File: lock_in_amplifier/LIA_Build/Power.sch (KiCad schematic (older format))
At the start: 52 parts, among them J1 vref-in, J2 vref, J3 V-IN, J4 GND, J5 V+IN, J6 +5V, J7 +3V3, J8 -5V, Q1 2N7000, Q2 2N7000, U1 OP1177, U2 ?, U3 ?, U4 ?

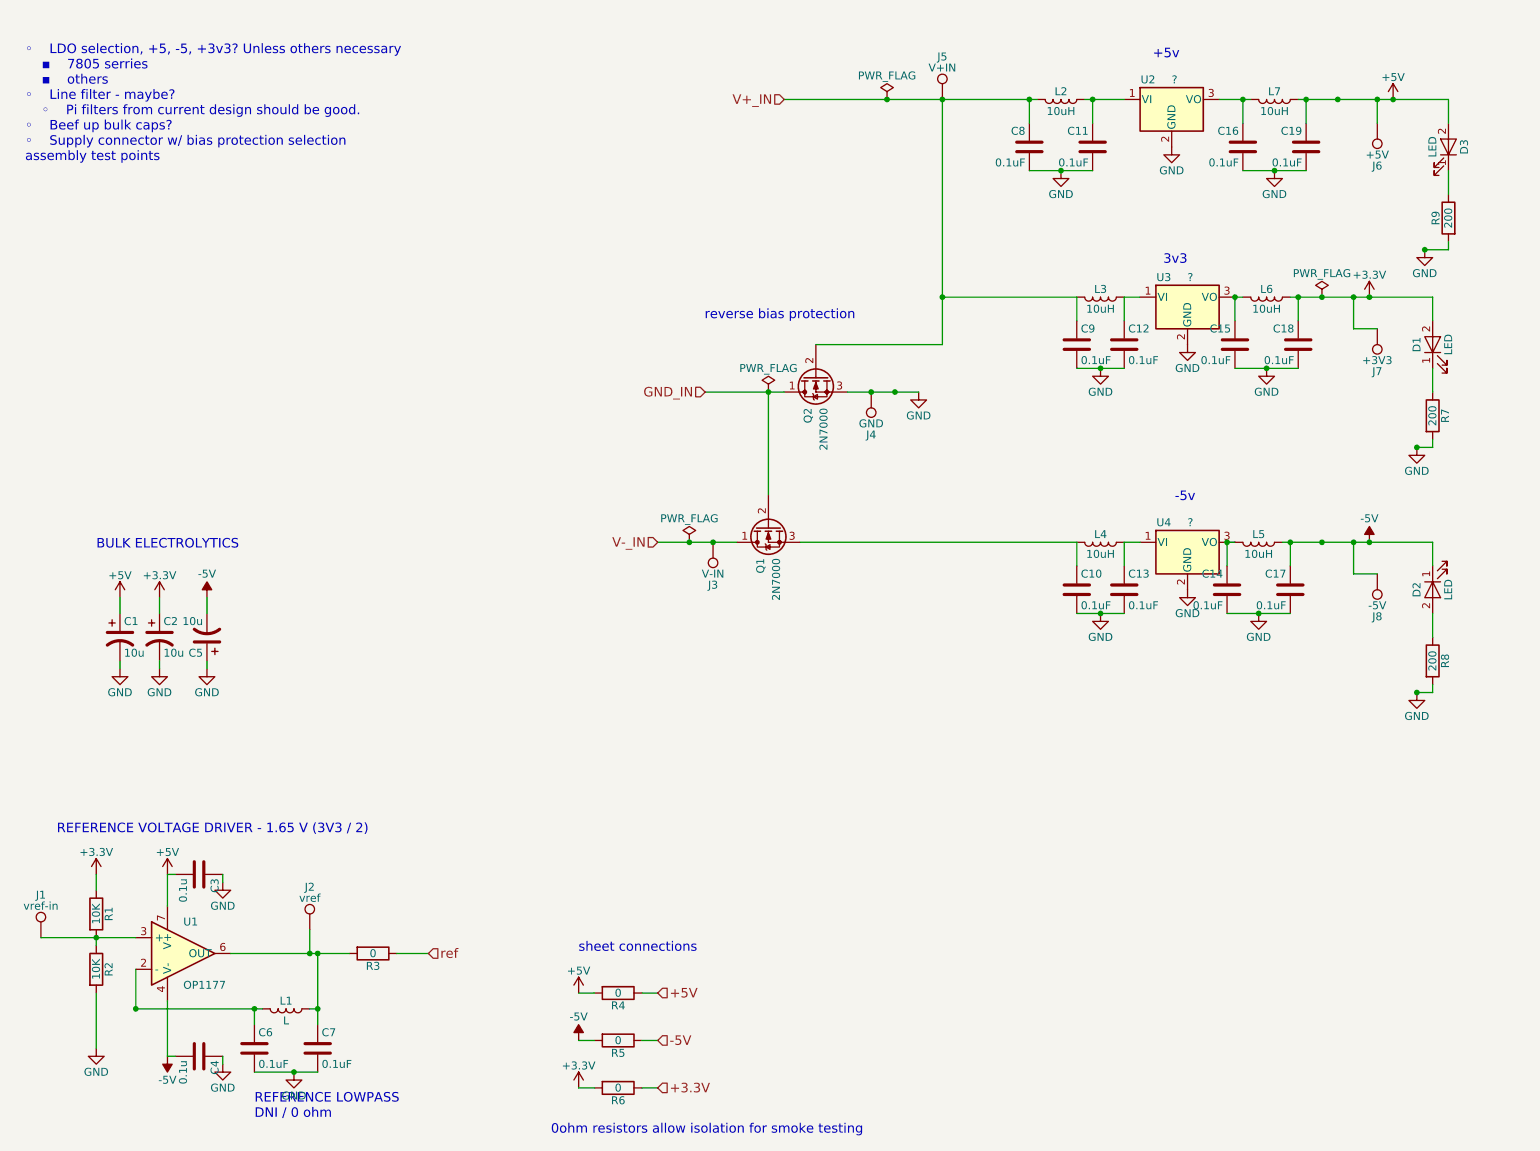
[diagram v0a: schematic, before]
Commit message: power supply, amp chain first pass
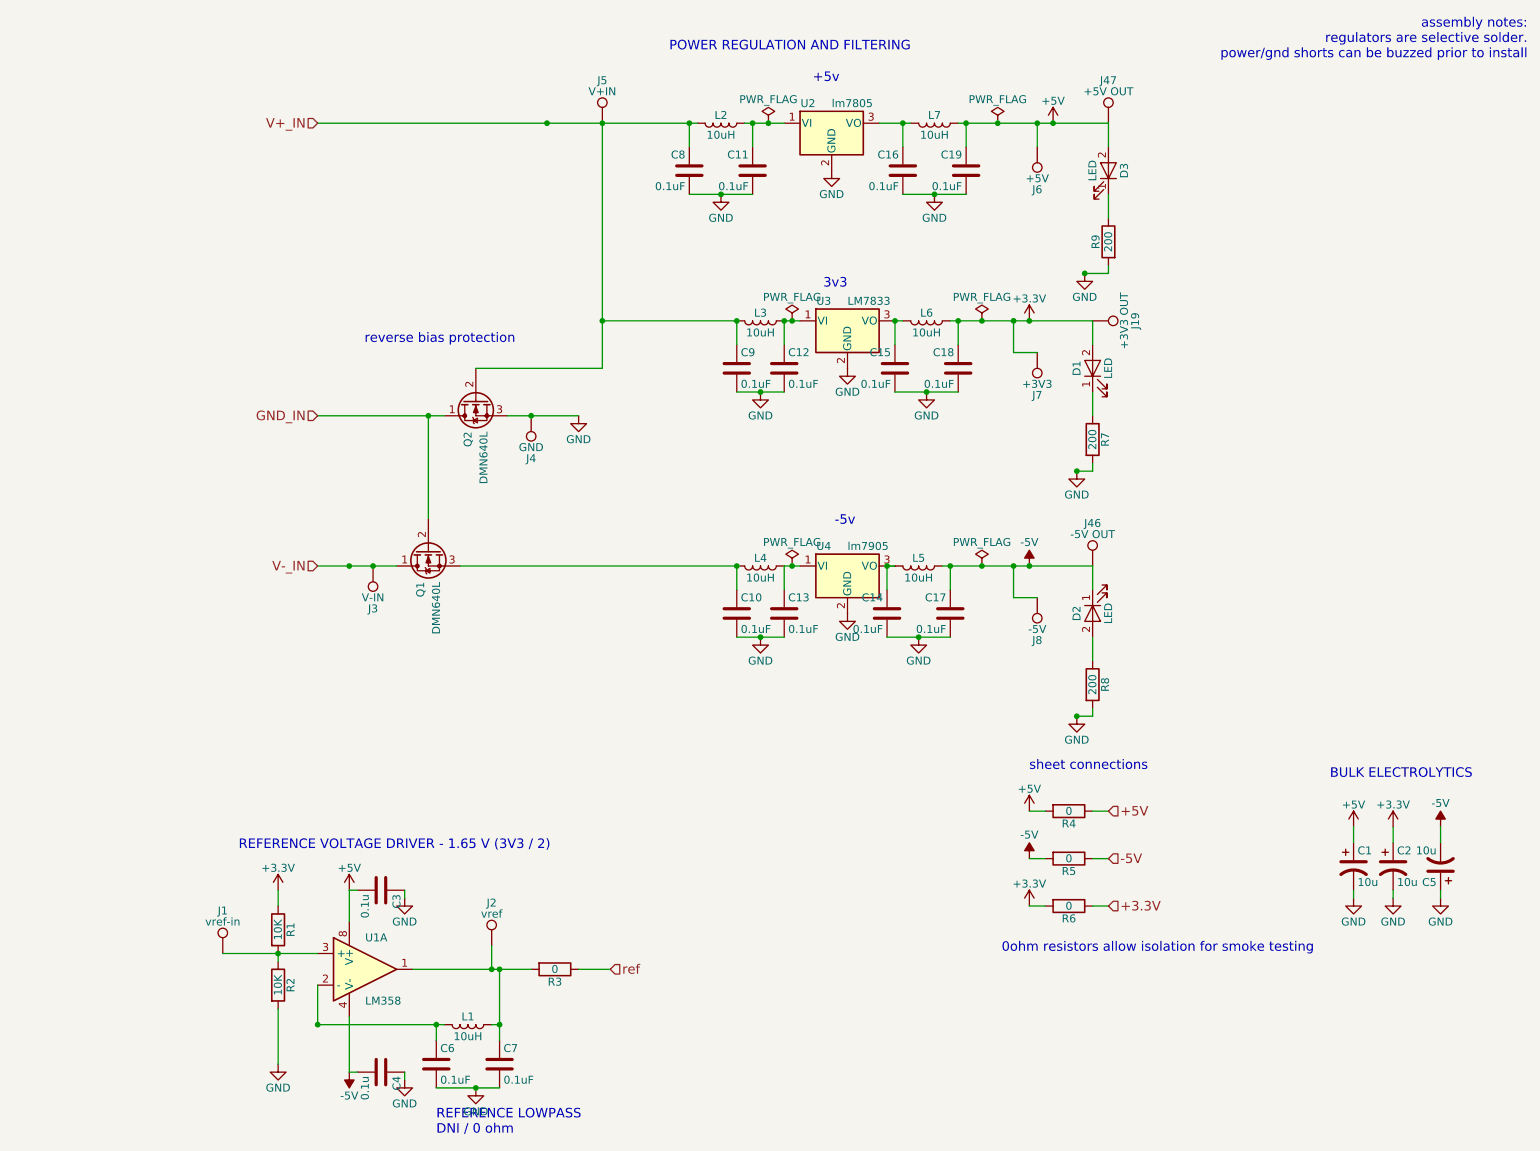
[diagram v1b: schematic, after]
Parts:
- removed U1: OP1177, Housings_SSOP:MSOP-8-1EP_3x3mm_Pitch0.65mm, symbol OP1177
- added J19: +3V3 OUT, footprints:tyco_RCU_0603_Probe_Pad, symbol TEST_1P
- added J46: -5V OUT, footprints:tyco_RCU_0603_Probe_Pad, symbol TEST_1P
- added J47: +5V OUT, footprints:tyco_RCU_0603_Probe_Pad, symbol TEST_1P
- added U1: LM358, symbol LM358
- C10, C11, C12, C13, C14, C15, C16, C17, C18, C19, C3, C4, C6, C7, C8, C9: footprint Capacitors_SMD:C_0805_HandSoldering -> Capacitors_SMD:C_0805
- J1, J2, J3, J4, J5, J6, J7, J8: footprint Measurement_Points:Measurement_Point_Round-SMD-Pad_Small -> footprints:tyco_RCU_0603_Probe_Pad
- L1: value L -> 10uH
- Q1, Q2: value 2N7000 -> DMN640L
- R1, R2, R7, R8, R9: footprint Resistors_SMD:R_0805_HandSoldering -> Resistors_SMD:R_0805
- R3, R4, R5, R6: footprint (none) -> Resistors_SMD:R_0805
- U2: value ? -> lm7805
- U3: value ? -> LM7833
- U4: value ? -> lm7905
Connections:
- net +3V3: now also J19.1
- net +5V: now also J47.1, U1.8 (V+)
- net -5V: now also J46.1, U1.4 (V-)
- net at J1.1, R1.2, R2.1: now also U1.3 (+)
- net at C7.1, J2.1, L1.1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: now also U1.1
- net at C6.1, L1.2: now also U1.2 (-)
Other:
- note added: "POWER REGULATION AND FILTERING"
- note added: "assembly notes:\nregulators are selective solder.\npower/gnd shorts can be buzzed prior to install\n"
- note removed: "◦ LDO selection, +5, -5, +3v3? Unless others necessary\n ▪ 7805 serries\n ▪ others\n◦ Line filter - maybe?\n ◦ Pi filters from current design should be good.\n◦ Beef up bulk caps?\n◦ Supply connector w/ bias protection selection\nassembly test points\n"
- moved on the sheet: C1, C10, C11, C12, C13, C14, C15, C16, C17, C18, C19, C2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

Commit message: initial transimpedance selection, lna refinement
amp overload led
switch comps added
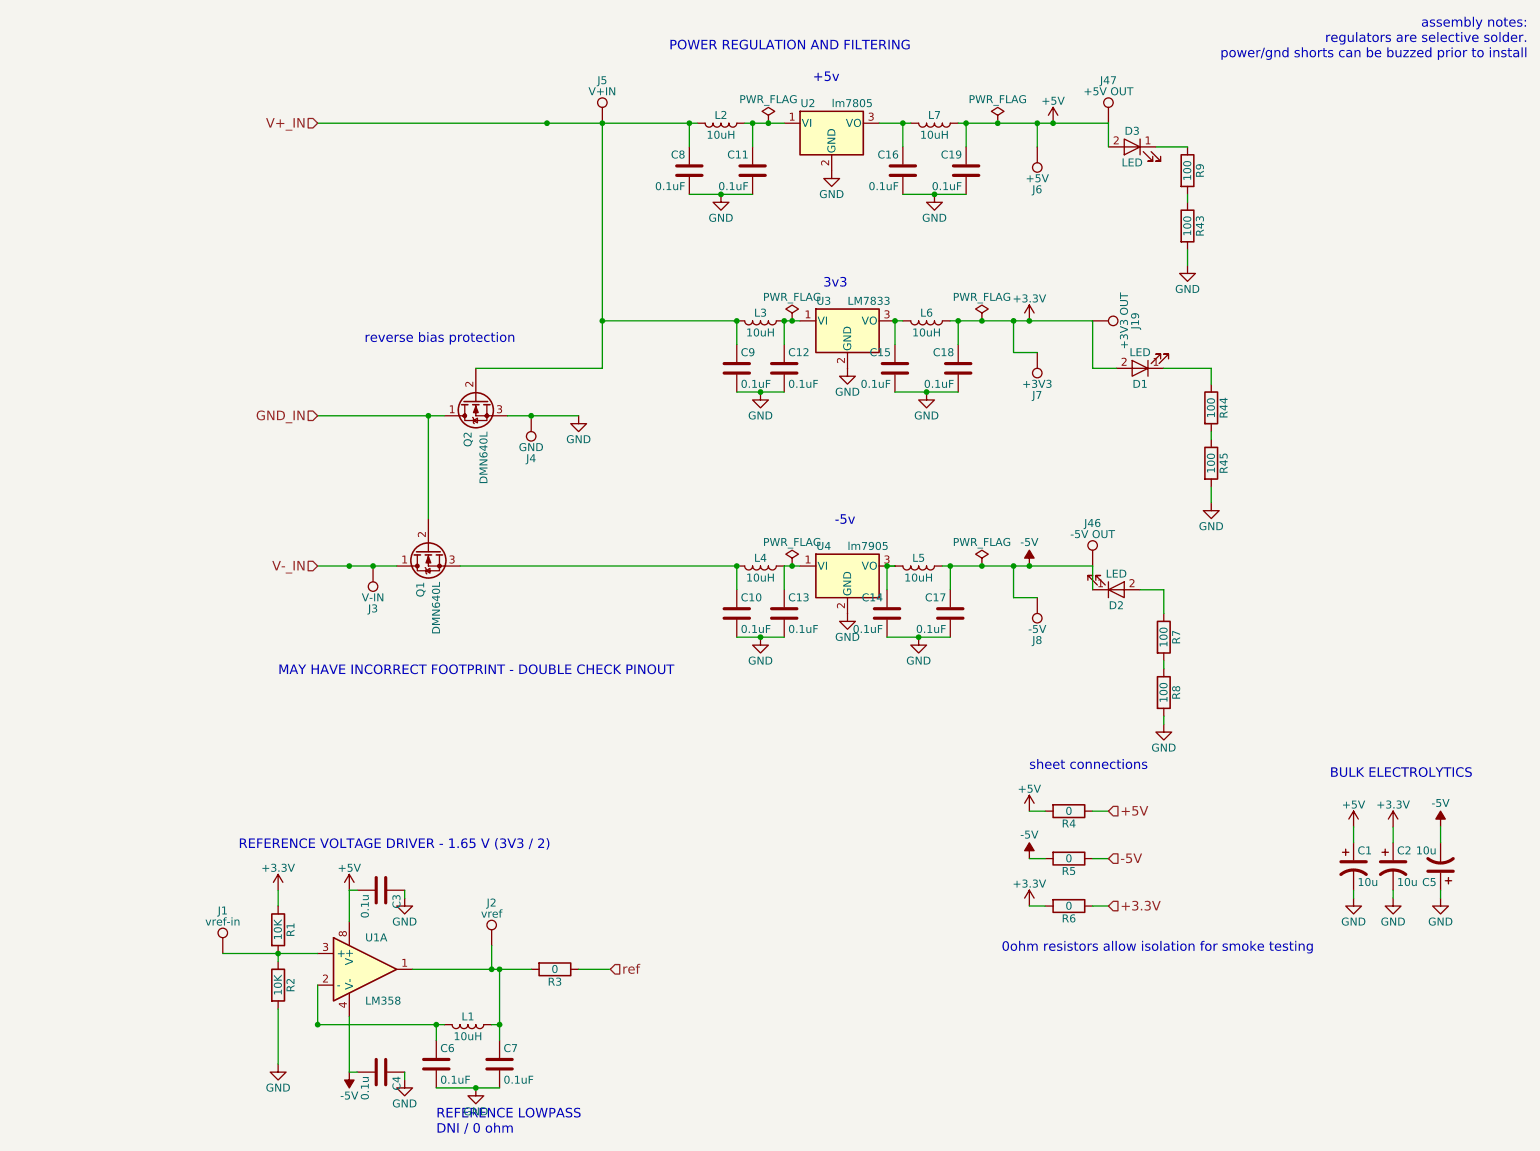
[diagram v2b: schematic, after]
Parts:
- added R43, R44, R45: 100, Resistors_SMD:R_0805, symbol R
- Q1, Q2: footprint (none) -> TO_SOT_Packages_SMD:SOT-23
- R7, R8, R9: value 200 -> 100
- U1: footprint (none) -> SMD_Packages:SOIC-8-N
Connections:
- net GND: now also R43.2, R45.2; no longer R7.2, R9.2
- net at D2.2 (A): now also R7.1; no longer R8.1
- net at D1.1 (K): now also R44.1; no longer R7.1
- new net: R43.1, R9.2
- new net: R44.2, R45.1
- new net: R7.2, R8.1
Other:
- note added: "MAY HAVE INCORRECT FOOTPRINT - DOUBLE CHECK PINOUT"
- moved on the sheet: D1, D2, D3
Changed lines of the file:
@@
 $Descr USLetter 11000 8500
 encoding utf-8
-Sheet 2 5
+Sheet 2 6
 Title "POWER REGULATION AND FILTERING"
 Date ""
@@
 L GND #PWR016
 U 1 1 5A1C8AA9
-P 7500 2300
-F 0 "#PWR016" H 7500 2050 50  0001 C CNN
-F 1 "GND" H 7500 2150 50  0000 C CNN
-F 2 "" H 7500 2300 50  0001 C CNN
-F 3 "" H 7500 2300 50  0001 C CNN
-	1    7500 2300
+P 8150 2250
+F 0 "#PWR016" H 8150 2000 50  0001 C CNN
+F 1 "GND" H 8150 2100 50  0000 C CNN
+F 2 "" H 8150 2250 50  0001 C CNN
+F 3 "" H 8150 2250 50  0001 C CNN
+	1    8150 2250
 	-1   0    0    -1
 $EndComp
@@
 L LED D3
 U 1 1 5A1C8B12
-P 7650 1650
-F 0 "D3" H 7650 1750 50  0000 C CNN
-F 1 "LED" H 7650 1550 50  0000 C CNN
-F 2 "Diodes_SMD:D_0805" H 7650 1650 50  0001 C CNN
-F 3 "" H 7650 1650 50  0001 C CNN
-	1    7650 1650
-	0    1    -1   0
+P 7800 1500
+F 0 "D3" H 7800 1600 50  0000 C CNN
+F 1 "LED" H 7800 1400 50  0000 C CNN
+F 2 "Diodes_SMD:D_0805" H 7800 1500 50  0001 C CNN
+F 3 "" H 7800 1500 50  0001 C CNN
+	1    7800 1500
+	-1   0    0    -1
 $EndComp
 $Comp
 L LED D2
 U 1 1 5A1C8B19
-P 7550 4450
-F 0 "D2" H 7550 4550 50  0000 C CNN
-F 1 "LED" H 7550 4350 50  0000 C CNN
-F 2 "Diodes_SMD:D_0805" H 7550 4450 50  0001 C CNN
-F 3 "" H 7550 4450 50  0001 C CNN
-	1    7550 4450
-	0    -1   1    0
-$EndComp
-$Comp
-L R R9
-U 1 1 5A1C8B20
-P 7650 2100
-F 0 "R9" V 7730 2100 50  0000 C CNN
-F 1 "200" V 7650 2100 50  0000 C CNN
-F 2 "Resistors_SMD:R_0805" V 7580 2100 50  0001 C CNN
-F 3 "" H 7650 2100 50  0001 C CNN
-	1    7650 2100
-	-1   0    0    -1
-$EndComp
-$Comp
-L R R8
-U 1 1 5A1C8B27
-P 7550 4900
-F 0 "R8" V 7630 4900 50  0000 C CNN
-F 1 "200" V 7550 4900 50  0000 C CNN
-F 2 "Resistors_SMD:R_0805" V 7480 4900 50  0001 C CNN
-F 3 "" H 7550 4900 50  0001 C CNN
-	1    7550 4900
-	1    0    0    -1
+P 7700 4300
+F 0 "D2" H 7700 4400 50  0000 C CNN
+F 1 "LED" H 7700 4200 50  0000 C CNN
+F 2 "Diodes_SMD:D_0805" H 7700 4300 50  0001 C CNN
+F 3 "" H 7700 4300 50  0001 C CNN
+	1    7700 4300
+	1    0    0    1
 $EndComp
 Wire Wire Line
@@
 Connection ~ 5450 4600
 Connection ~ 5000 1350
-Wire Wire Line
-	7650 1800 7650 1950
-Wire Wire Line
-	7550 4600 7550 4750
-Wire Wire Line
-	7550 5100 7550 5050
-Wire Wire Line
-	7650 2300 7500 2300
-Wire Wire Line
-	7450 5100 7550 5100
-Wire Wire Line
-	7650 2250 7650 2300
-Connection ~ 7500 2300
-Connection ~ 7450 5100
 Wire Wire Line
 	7550 4150 7550 4300
@@
 F 0 "Q2" H 3850 3150 50  0000 L CNN
 F 1 "DMN640L" H 3850 3050 50  0000 L CNN
-F 2 "" H 3850 3200 50  0001 C CNN
+F 2 "TO_SOT_Packages_SMD:SOT-23" H 3850 3200 50  0001 C CNN
 F 3 "" H 3650 3100 50  0001 C CNN
 	1    3650 3100
@@
 F 0 "Q1" H 3550 4100 50  0000 L CNN
 F 1 "DMN640L" H 3550 4000 50  0000 L CNN
-F 2 "" H 3550 4150 50  0001 C CNN
+F 2 "TO_SOT_Packages_SMD:SOT-23" H 3550 4150 50  0001 C CNN
 F 3 "" H 3350 4050 50  0001 C CNN
 	1    3350 4050
@@
 L GND #PWR026
 U 1 1 5A1CCB9E
-P 7450 5100
-F 0 "#PWR026" H 7450 4850 50  0001 C CNN
-F 1 "GND" H 7450 4950 50  0000 C CNN
-F 2 "" H 7450 5100 50  0001 C CNN
-F 3 "" H 7450 5100 50  0001 C CNN
-	1    7450 5100
+P 8000 5150
+F 0 "#PWR026" H 8000 4900 50  0001 C CNN
+F 1 "GND" H 8000 5000 50  0000 C CNN
+F 2 "" H 8000 5150 50  0001 C CNN
+F 3 "" H 8000 5150 50  0001 C CNN
+	1    8000 5150
 	1    0    0    -1
 $EndComp
@@
 L LED D1
 U 1 1 5A1CFB76
-P 7550 2900
-F 0 "D1" H 7550 3000 50  0000 C CNN
-F 1 "LED" H 7550 2800 50  0000 C CNN
-F 2 "Diodes_SMD:D_0805" H 7550 2900 50  0001 C CNN
-F 3 "" H 7550 2900 50  0001 C CNN
-	1    7550 2900
-	0    -1   -1   0
-$EndComp
-$Comp
-L R R7
-U 1 1 5A1CFB7D
-P 7550 3350
-F 0 "R7" V 7630 3350 50  0000 C CNN
-F 1 "200" V 7550 3350 50  0000 C CNN
-F 2 "Resistors_SMD:R_0805" V 7480 3350 50  0001 C CNN
-F 3 "" H 7550 3350 50  0001 C CNN
-	1    7550 3350
-	1    0    0    -1
+P 7850 2900
+F 0 "D1" H 7850 3000 50  0000 C CNN
+F 1 "LED" H 7850 2800 50  0000 C CNN
+F 2 "Diodes_SMD:D_0805" H 7850 2900 50  0001 C CNN
+F 3 "" H 7850 2900 50  0001 C CNN
+	1    7850 2900
+	-1   0    0    1
 $EndComp
 Wire Wire Line
@@
 Connection ~ 5450 3050
 Wire Wire Line
-	7550 3050 7550 3200
-Wire Wire Line
-	7550 3550 7550 3500
-Wire Wire Line
-	7450 3550 7550 3550
-Connection ~ 7450 3550
-Wire Wire Line
-	7550 2600 7550 2750
+	7550 2600 7550 2900
 Wire Wire Line
 	5600 2600 5700 2600
@@
 L GND #PWR032
 U 1 1 5A1CFB9A
-P 7450 3550
-F 0 "#PWR032" H 7450 3300 50  0001 C CNN
-F 1 "GND" H 7450 3400 50  0000 C CNN
-F 2 "" H 7450 3550 50  0001 C CNN
-F 3 "" H 7450 3550 50  0001 C CNN
-	1    7450 3550
+P 8300 3750
+F 0 "#PWR032" H 8300 3500 50  0001 C CNN
+F 1 "GND" H 8300 3600 50  0000 C CNN
+F 2 "" H 8300 3750 50  0001 C CNN
+F 3 "" H 8300 3750 50  0001 C CNN
+	1    8300 3750
 	1    0    0    -1
 $EndComp
@@
 F 0 "U1" H 2950 6900 50  0000 L CNN
 F 1 "LM358" H 2950 6500 50  0000 L CNN
-F 2 "" H 2950 6700 50  0001 C CNN
+F 2 "SMD_Packages:SOIC-8-N" H 2950 6700 50  0001 C CNN
 F 3 "" H 2950 6700 50  0001 C CNN
 	1    2950 6700
 	1    0    0    -1
 $EndComp
+Text Notes 2400 4850 0    60   ~ 0
+MAY HAVE INCORRECT FOOTPRINT - DOUBLE CHECK PINOUT
+$Comp
+L R R9
+U 1 1 5A270F3A
+P 8150 1650
+F 0 "R9" V 8230 1650 50  0000 C CNN
+F 1 "100" V 8150 1650 50  0000 C CNN
+F 2 "Resistors_SMD:R_0805" V 8080 1650 50  0001 C CNN
+F 3 "" H 8150 1650 50  0001 C CNN
+	1    8150 1650
+	1    0    0    -1
+$EndComp
+$Comp
+L R R43
+U 1 1 5A27106D
+P 8150 2000
+F 0 "R43" V 8230 2000 50  0000 C CNN
+F 1 "100" V 8150 2000 50  0000 C CNN
+F 2 "Resistors_SMD:R_0805" V 8080 2000 50  0001 C CNN
+F 3 "" H 8150 2000 50  0001 C CNN
+	1    8150 2000
+	1    0    0    -1
+$EndComp
+$Comp
+L R R44
+U 1 1 5A27115B
+P 8300 3150
+F 0 "R44" V 8380 3150 50  0000 C CNN
+F 1 "100" V 8300 3150 50  0000 C CNN
+F 2 "Resistors_SMD:R_0805" V 8230 3150 50  0001 C CNN
+F 3 "" H 8300 3150 50  0001 C CNN
+	1    8300 3150
+	1    0    0    -1
+$EndComp
+$Comp
+L R R45
+U 1 1 5A271161
+P 8300 3500
+F 0 "R45" V 8380 3500 50  0000 C CNN
+F 1 "100" V 8300 3500 50  0000 C CNN
+F 2 "Resistors_SMD:R_0805" V 8230 3500 50  0001 C CNN
+F 3 "" H 8300 3500 50  0001 C CNN
+	1    8300 3500
+	1    0    0    -1
+$EndComp
+$Comp
+L R R7
+U 1 1 5A271287
+P 8000 4600
+F 0 "R7" V 8080 4600 50  0000 C CNN
+F 1 "100" V 8000 4600 50  0000 C CNN
+F 2 "Resistors_SMD:R_0805" V 7930 4600 50  0001 C CNN
+F 3 "" H 8000 4600 50  0001 C CNN
+	1    8000 4600
+	1    0    0    -1
+$EndComp
+$Comp
+L R R8
+U 1 1 5A27128D
+P 8000 4950
+F 0 "R8" V 8080 4950 50  0000 C CNN
+F 1 "100" V 8000 4950 50  0000 C CNN
+F 2 "Resistors_SMD:R_0805" V 7930 4950 50  0001 C CNN
+F 3 "" H 8000 4950 50  0001 C CNN
+	1    8000 4950
+	1    0    0    -1
+$EndComp
+Wire Wire Line
+	7950 1500 8150 1500
+Wire Wire Line
+	8150 1800 8150 1850
+Wire Wire Line
+	8150 2150 8150 2250
+Wire Wire Line
+	7550 2900 7700 2900
+Wire Wire Line
+	8000 2900 8300 2900
+Wire Wire Line
+	8300 2900 8300 3000
+Wire Wire Line
+	8300 3300 8300 3350
+Wire Wire Line
+	8300 3650 8300 3750
+Wire Wire Line
+	7850 4300 8000 4300
+Wire Wire Line
+	8000 4300 8000 4450
+Wire Wire Line
+	8000 4750 8000 4800
+Wire Wire Line
+	8000 5150 8000 5100
 $EndSCHEMATC
